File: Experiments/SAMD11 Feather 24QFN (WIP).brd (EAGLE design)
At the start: 50.8 x 22.9 mm, 30 parts, among them IC1 ATSAMD11D14A-SSNT, J1 10118193-0001LF, Q1 DMG341, SW1 SPST_TACT-KMR2, U1 AP2112-3.3, U2 MCP73831T-2ACI/OT, X1 JSTPH, X2 2x5 0.05" SWD

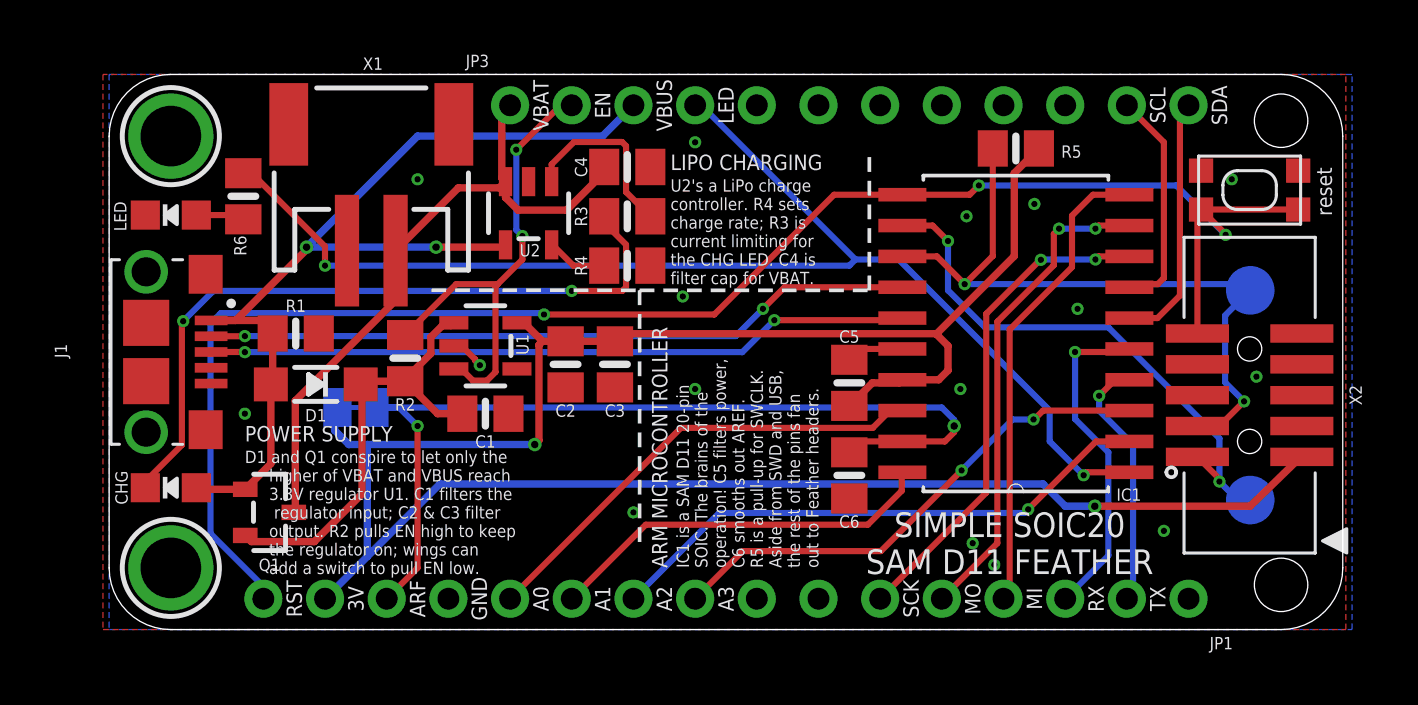
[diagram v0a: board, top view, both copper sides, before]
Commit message: first rev of the hand-solderable one, WIP the QFN package
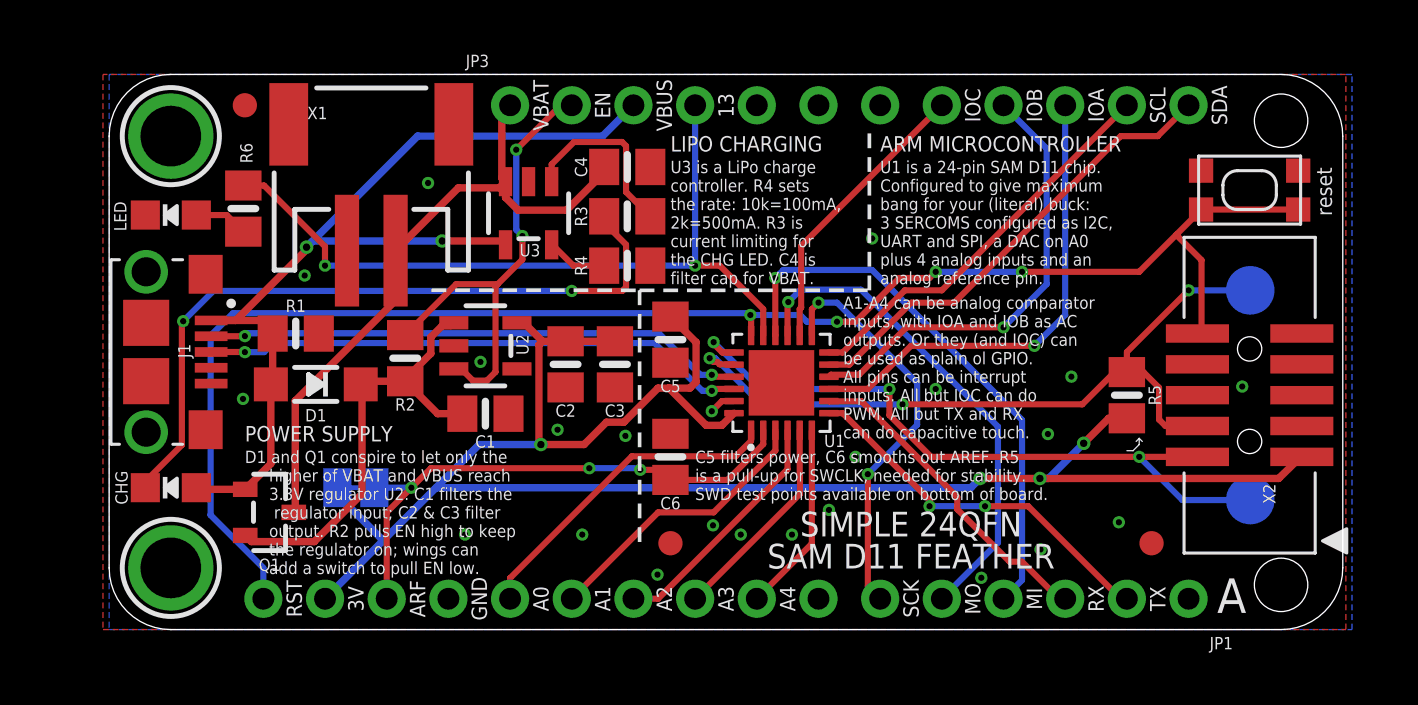
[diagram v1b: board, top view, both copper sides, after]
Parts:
- removed IC1: ATSAMD11D14A-SSNT, ATSAMD11D14A-SSNT:SOIC127P1030X265-20N
- added FID1, FID3, FID4: FIDUCIAL_1MM, microbuilder:FIDUCIAL_1MM
- added GOLD_ORB_SM1: OSHWLOGOLOGO5MM, oshw:OSHW_5MM
- added U3: MCP73831T-2ACI/OT, microbuilder:SOT23-5
- U1: value AP2112-3.3 -> ATSAMD11D14A-MUT; device microbuilder:SOT23-5 -> ATSAMD11D14A-MUT:QFN50P400X400X90-25N
- U2: value MCP73831T-2ACI/OT -> AP2112-3.3
- moved U1 12.3 mm to (27.7, 10.2), turned to 90 degrees
- moved R5 11.1 mm to (41.9, 9.65), turned to 270 degrees
- moved C5 7.58 mm to (23.1, 11.9), turned to 270 degrees
- moved C6 7.41 mm to (23.1, 7.11), turned to 90 degrees
- moved U2 5.74 mm to (15.5, 11.7), turned to 270 degrees
- moved SJ1 3.30 mm to (10.2, 5.84)
- moved R6 0.51 mm to (5.52, 17.3)
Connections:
- net !RESET: now also U1.18; no longer IC1.11
- net +3V3: now also U1.24, U2.5; no longer IC1.17, U1.5
- net A0: now also U1.1; no longer IC1.18
- net A1: now also U1.3; no longer IC1.20
- net A2: now also U1.4; no longer IC1.2
- net A3: now also U1.5; no longer IC1.3
- net A4: now also U1.6
- net AREF: now also U1.2; no longer IC1.19
- net EN: now also U2.3; no longer U1.3
- net GND: now also U1.23, U3.2; no longer IC1.16, U1.2
- net IOA: now also U1.9
- net IOB: now also U1.10
- net IOC: now also U1.14
- net LED: now also U1.17; no longer IC1.1
- net MISO: now also U1.16; no longer IC1.10
- net MOSI: now also U1.15; no longer IC1.9
- net PROG: now also U3.5; no longer U2.5
- net RX: now also U1.8; no longer IC1.5
- net SCK: now also U1.13; no longer IC1.8
- net SCL: now also U1.12; no longer IC1.7
- net SDA: now also U1.11; no longer IC1.6
- net STAT: now also U3.1; no longer U2.1
- net SWCLK: now also U1.20; no longer IC1.13
- net SWDIO: now also U1.19; no longer IC1.12
- net TX: now also U1.7; no longer IC1.4
- net USB_N: now also U1.21; no longer IC1.14
- net USB_P: now also U1.22; no longer IC1.15
- net VBAT: now also U3.3; no longer U2.3
- net VBUS: now also U3.4; no longer U2.4
- net VHI: now also U2.1; no longer U1.1
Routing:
- net LED: track 52.3 -> 31.7 mm
- net IOA: track 0.00 -> 19.6 mm, vias 0 -> 1
- net IOB: track 0.00 -> 18.6 mm, vias 0 -> 1
- net +3V3: track 95.3 -> 78.1 mm, vias 2 -> 4
- net AREF: track 39.0 -> 22.7 mm, vias 2 -> 3
- net A2: track 23.1 -> 10.2 mm, vias 1 -> 0
- net A3: track 21.1 -> 8.73 mm, vias 2 -> 0
- net IOC: track 0.00 -> 11.9 mm
- net SDA: track 10.5 -> 19.2 mm
- net A4: track 0.00 -> 7.87 mm
- net SCL: track 9.32 -> 16.5 mm
- net USB_N: track 29.3 -> 22.4 mm
- net USB_P: track 29.0 -> 22.6 mm
- net SWDIO: track 22.6 -> 28.9 mm, vias 2 -> 3
- net A0: track 19.4 -> 13.6 mm
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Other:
- board text added: "13"
- board text added: "13/LED PA05"
- board text added: "A"
- board text added: "A1-A4 can be analog comparator inputs, with IOA and IOB as AC outputs. Or they (and IOC) can be used as plain ol GPIO. All pins can be interrupt inputs. All but IOC can do PWM. All but TX and RX can do capacitive touch."
- board text added: "A4"
- board text added: "C5 filters power, C6 smooths out AREF. R5 is a pull-up for SWCLK, needed for stability. SWD test points available on bottom of board."
- board text added: "D1 and Q1 conspire to let only the higher of VBAT and VBUS reach 3.3V regulator U2. C1 filters the regulator input; C2 & C3 filter output. R2 pulls EN high to keep the regulator on; wings can add a switch to pull EN low."
- board text added: "IOA"
- board text added: "IOB"
- board text added: "IOC"
- board text added: "SIMPLE 24QFN SAM D11 FEATHER"
- board text added: "Simple 24QFN SAM D11 Feather"
- board text added: "U1 is a 24-pin SAM D11 chip. Configured to give maximum bang for your (literal) buck: 3 SERCOMS configured as I2C, UART and SPI, a DAC on A0 plus 4 analog inputs and an analog reference pin."
- board text added: "U3 is a LiPo charge controller. R4 sets the rate: 10k=100mA, 2k=500mA. R3 is current limiting for the CHG LED. C4 is filter cap for VBAT."
- board text removed: "D1 and Q1 conspire to let only the higher of VBAT and VBUS reach 3.3V regulator U1. C1 filters the regulator input; C2 & C3 filter output. R2 pulls EN high to keep the regulator on; wings can add a switch to pull EN low."
- board text removed: "IC1 is a SAM D11 20-pin SOIC. The brains of the operation! C5 filters power, C6 smooths out AREF. R5 is a pull-up for SWCLK. Aside from SWD and USB, the rest of the pins fan out to Feather headers."
- board text removed: "LED"
- board text removed: "LED PA05"
- board text removed: "RST PA28"
- board text removed: "SIMPLE SOIC20 SAM D11 FEATHER"
- board text removed: "Simple SOIC-20 SAM D11 Feather"
- board text removed: "U2's a LiPo charge controller. R4 sets charge rate; R3 is current limiting for the CHG LED. C4 is filter cap for VBAT."

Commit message: tweak some silkscreen text
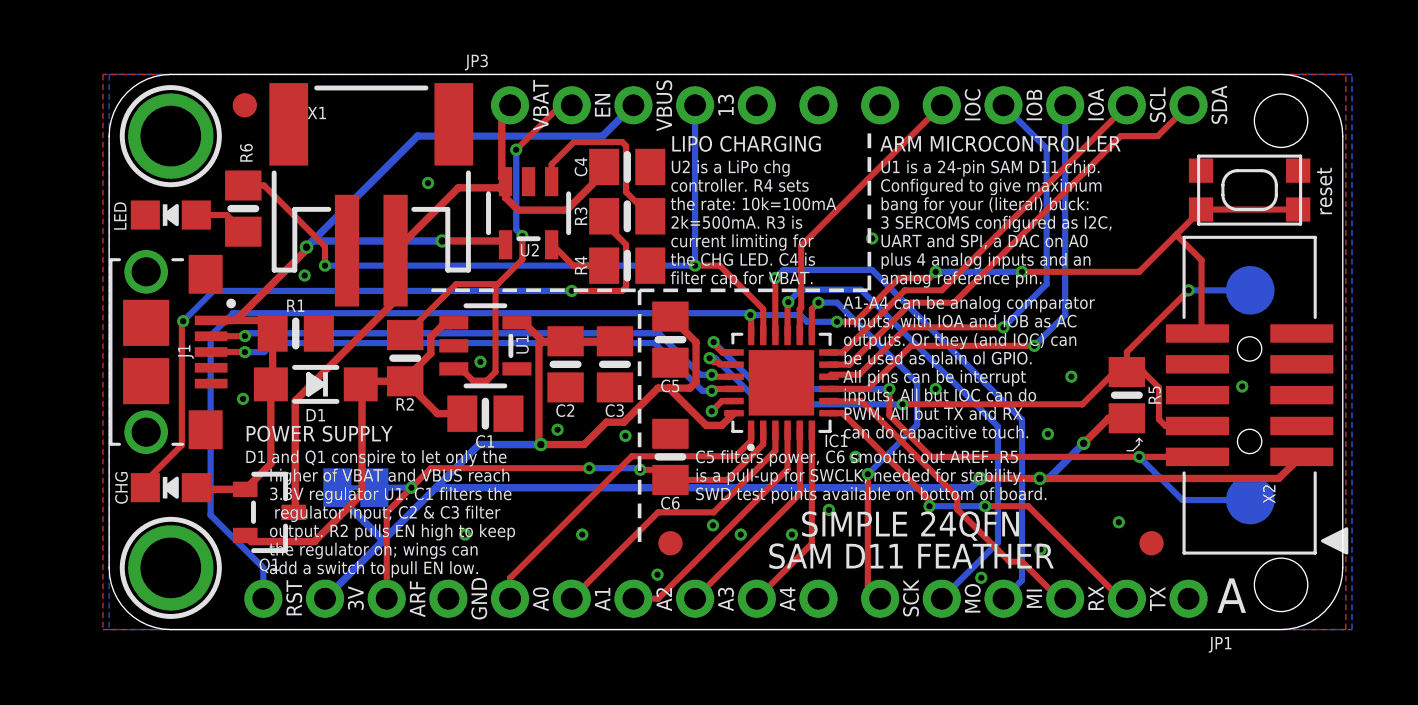
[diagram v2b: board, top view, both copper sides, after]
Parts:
- removed U3: MCP73831T-2ACI/OT, microbuilder:SOT23-5
- added IC1: ATSAMD11D14A-MUT, ATSAMD11D14A-MUT:QFN50P400X400X90-25N
- U1: value ATSAMD11D14A-MUT -> AP2112-3.3; device ATSAMD11D14A-MUT:QFN50P400X400X90-25N -> microbuilder:SOT23-5
- U2: value AP2112-3.3 -> MCP73831T-2ACI/OT
- moved U1 12.3 mm to (15.5, 11.7), turned to 270 degrees
- moved U2 5.74 mm to (17.3, 17.1), turned to 180 degrees
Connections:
- net !RESET: now also IC1.18; no longer U1.18
- net +3V3: now also IC1.24, U1.5; no longer U1.24, U2.5
- net A0: now also IC1.1; no longer U1.1
- net A1: now also IC1.3; no longer U1.3
- net A2: now also IC1.4; no longer U1.4
- net A3: now also IC1.5; no longer U1.5
- net A4: now also IC1.6; no longer U1.6
- net AREF: now also IC1.2; no longer U1.2
- net EN: now also U1.3; no longer U2.3
- net GND: now also IC1.23, U1.2; no longer U1.23, U3.2
- net IOA: now also IC1.9; no longer U1.9
- net IOB: now also IC1.10; no longer U1.10
- net IOC: now also IC1.14; no longer U1.14
- net LED: now also IC1.17; no longer U1.17
- net MISO: now also IC1.16; no longer U1.16
- net MOSI: now also IC1.15; no longer U1.15
- net PROG: now also U2.5; no longer U3.5
- net RX: now also IC1.8; no longer U1.8
- net SCK: now also IC1.13; no longer U1.13
- net SCL: now also IC1.12; no longer U1.12
- net SDA: now also IC1.11; no longer U1.11
- net STAT: now also U2.1; no longer U3.1
- net SWCLK: now also IC1.20; no longer U1.20
- net SWDIO: now also IC1.19; no longer U1.19
- net TX: now also IC1.7; no longer U1.7
- net USB_N: now also IC1.21; no longer U1.21
- net USB_P: now also IC1.22; no longer U1.22
- net VBAT: now also U2.3; no longer U3.3
- net VBUS: now also U2.4; no longer U3.4
- net VHI: now also U1.1; no longer U2.1
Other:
- board text added: "A2 PA05"
- board text added: "A3 PA06"
- board text added: "A4 PA07"
- board text added: "D1 and Q1 conspire to let only the higher of VBAT and VBUS reach 3.3V regulator U1. C1 filters the regulator input; C2 & C3 filter output. R2 pulls EN high to keep the regulator on; wings can add a switch to pull EN low."
- board text added: "IOA PA10"
- board text added: "IOB PA11"
- board text added: "IOC PA17"
- board text added: "LED PA27"
- board text added: "U2 is a LiPo chg controller. R4 sets the rate: 10k=100mA 2k=500mA. R3 is current limiting for the CHG LED. C4 is filter cap for VBAT."
- board text removed: "13/LED PA05"
- board text removed: "A2 PA06"
- board text removed: "A3 PA07"
- board text removed: "D1 and Q1 conspire to let only the higher of VBAT and VBUS reach 3.3V regulator U2. C1 filters the regulator input; C2 & C3 filter output. R2 pulls EN high to keep the regulator on; wings can add a switch to pull EN low."
- board text removed: "U3 is a LiPo charge controller. R4 sets the rate: 10k=100mA, 2k=500mA. R3 is current limiting for the CHG LED. C4 is filter cap for VBAT."

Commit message: silkscreen tweaks
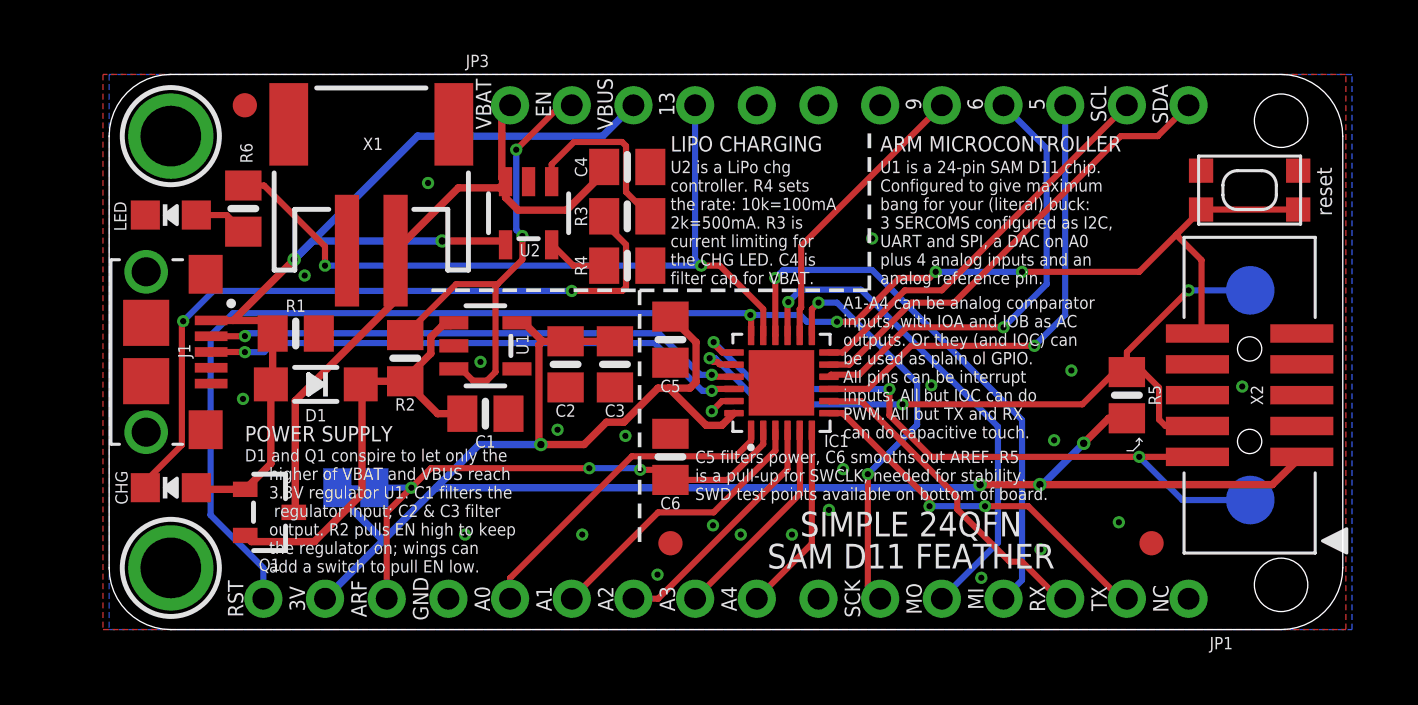
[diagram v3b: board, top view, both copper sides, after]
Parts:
- added U$2: OSO_BEAR, My Stuff:OSO_BEAR_750MIL
- added U$3: OSO_GRAPHIC, My Stuff:OSO_GRAPHIC
- added U$5: OSO_TEXTOSO_TEXT_ONELINE_125MIL, My Stuff:OSO_ONELINE_125MIL
- turned GOLD_ORB_SM1 to 270 degrees
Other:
- board text added: "13/LED PA27"
- board text added: "5"
- board text added: "5 PA10"
- board text added: "6"
- board text added: "6 PA11"
- board text added: "9"
- board text added: "9 PA17"
- board text added: "NC"
- board text added: "OSO-SAFE-B1-01"
- board text added: "Open Source HW CC-BY-SA 4.0"
- board text added: "plz don't steal the bear tho."
- board text removed: "@josecastillo"
- board text removed: "IOA"
- board text removed: "IOA PA10"
- board text removed: "IOB"
- board text removed: "IOB PA11"
- board text removed: "IOC"
- board text removed: "IOC PA17"
- board text removed: "LED PA27"
